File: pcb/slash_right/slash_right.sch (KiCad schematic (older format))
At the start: 6 parts

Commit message: pcb: slash_right: General electronics
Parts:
- added C? (x5): 100n, symbol Device:C
- added C? (x2): 22p, symbol Device:C_Small
- added C?: 1u, symbol Device:C
- added C?: CP, symbol Device:CP
- added D?: D_Small, symbol Device:D_Small
- added D?: LED, symbol Device:LED
- added R? (x2): 10K, symbol Device:R_Small
- added R? (x2): 22, symbol Device:R_Small
- added R?: 470, symbol Device:R_Small
- added R? (x2): 4.7K, symbol Device:R_Small
- added SW?: SW_Push, symbol Switch:SW_Push
- added U?: ATmega32U4-AU, Package_QFP:TQFP-44_10x10mm_P0.8mm, symbol MCU_Microchip_ATmega:ATmega32U4-AU
- added Y?: 16MHz, symbol Device:Crystal
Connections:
- net +5V: now also J?.3, C?.1, C?.1, C?.1, C?.1, C?.1, C?.1, D?.1 (K), R?.1, R?.1, R?.1, U?.14 (VCC), U?.2 (UVCC), U?.24 (AVCC), U?.34 (VCC), U?.44 (AVCC), U?.7 (VBUS)
- net D+: now also R?.2
- net D-: now also R?.2
- net GND: now also J?.5, C?.1, C?.2, C?.2, C?.2, C?.2, C?.2, C?.2, C?.2, C?.2, D?.1 (K), R?.1, SW?.1, U?.15 (GND), U?.23 (GND), U?.35 (GND), U?.43 (GND), U?.5 (UGND)
- net SCL: now also J?.4, R?.2, U?.18 (PD0)
- net SDA: now also J?.2, R?.2, U?.19 (PD1)
- net MISO: now reaches J?.1 (MISO)
- net MISO: now also U?.11 (PB3)
- net SCK: now reaches J?.3 (SCK)
- net SCK: now also U?.9 (PB1)
- net MOSI: now reaches J?.4 (MOSI)
- net MOSI: now also U?.10 (PB2)
- net ~RST: now reaches J?.5 (~RST)
- net ~RST: now also D?.2 (A), R?.2, SW?.2, U?.13 (~RESET)
- new net: R?.1, U?.1 (PE6)
- new net: C?.2, U?.16 (XTAL2), Y?.2
- new net: C?.1, U?.17 (XTAL1), Y?.1
- new net: R?.2, U?.33 (~HWB~/PE2)
- new net: C?.1, U?.6 (UCAP)
- new net: D?.2 (A), R?.2
- new net D1+: R?.1, U?.4 (D+)
- new net D1-: R?.1, U?.3 (D-)
- no-connect marks 3 -> 4

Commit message: pcb: slash: Matrix schematic
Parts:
- added D? (x55): D_Small, symbol Device:D_Small
- added SW? (x55): SW_Push_45deg, symbol Switch:SW_Push_45deg
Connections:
- net COL7: now reaches U?.12 (PB7)
- net COL7: now also SW?.2, SW?.2, SW?.2
- net COL10: now reaches U?.20 (PD2)
- net COL10: now also SW?.2, SW?.2, SW?.2
- net COL11: now reaches U?.21 (PD3)
- net COL11: now also SW?.2, SW?.2, SW?.2
- net COL13: now reaches U?.22 (PD5)
- net COL13: now also SW?.2, SW?.2, SW?.2
- net COL12: now reaches U?.25 (PD4)
- net COL12: now also SW?.2, SW?.2, SW?.2
- net COL14: now reaches U?.26 (PD6)
- net COL14: now also SW?.2, SW?.2, SW?.2
- net COL15: now reaches U?.27 (PD7)
- net COL15: now also SW?.2, SW?.2, SW?.2
- net COL4: now reaches U?.28 (PB4)
- net COL4: now also SW?.2, SW?.2, SW?.2
- net COL5: now reaches U?.29 (PB5)
- net COL5: now also SW?.2, SW?.2, SW?.2
- net COL6: now reaches U?.30 (PB6)
- net COL6: now also SW?.2, SW?.2, SW?.2
- net COL8: now reaches U?.31 (PC6)
- net COL8: now also SW?.2, SW?.2, SW?.2
- net COL9: now reaches U?.32 (PC7)
- net COL9: now also SW?.2, SW?.2, SW?.2
- net ROW2: now reaches U?.36 (PF7)
- net ROW2: now also D?.1 (K), D?.1 (K), D?.1 (K), D?.1 (K), D?.1 (K), D?.1 (K), D?.1 (K), D?.1 (K), D?.1 (K), D?.1 (K), D?.1 (K), D?.1 (K), D?.1 (K), D?.1 (K), D?.1 (K), D?.1 (K), D?.1 (K), D?.1 (K), D?.1 (K)
- net ROW1: now reaches U?.37 (PF6)
- net ROW1: now also D?.1 (K), D?.1 (K), D?.1 (K), D?.1 (K), D?.1 (K), D?.1 (K), D?.1 (K), D?.1 (K), D?.1 (K), D?.1 (K), D?.1 (K), D?.1 (K), D?.1 (K), D?.1 (K), D?.1 (K), D?.1 (K), D?.1 (K)
- net ROW0: now reaches U?.38 (PF5)
- net ROW0: now also D?.1 (K), D?.1 (K), D?.1 (K), D?.1 (K), D?.1 (K), D?.1 (K), D?.1 (K), D?.1 (K), D?.1 (K), D?.1 (K), D?.1 (K), D?.1 (K), D?.1 (K), D?.1 (K), D?.1 (K), D?.1 (K), D?.1 (K), D?.1 (K), D?.1 (K)
- net COL18: now reaches U?.39 (PF4)
- net COL18: now also SW?.2, SW?.2
- net COL17: now reaches U?.40 (PF1)
- net COL17: now also SW?.2, SW?.2, SW?.2
- net COL16: now reaches U?.41 (PF0)
- net COL16: now also SW?.2, SW?.2
- net COL0: now reaches U?.8 (PB0)
- net COL0: now also SW?.2, SW?.2, SW?.2
- net MISO renamed COL3
- net COL3: now also SW?.2, SW?.2, SW?.2
- net MOSI renamed COL2
- net COL2: now also SW?.2, SW?.2, SW?.2
- net SCK renamed COL1
- net COL1: now also SW?.2, SW?.2, SW?.2
- new net: D?.2 (A), SW?.1 (x55)

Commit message: pcb: slash_righ: Fill missing values
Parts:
- C?: value CP -> 10uF
- F?: value Polyfuse -> 500mA
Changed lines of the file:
@@
 P 1450 950
 F 0 "F?" V 1225 950 50  0000 C CNN
-F 1 "Polyfuse" V 1316 950 50  0000 C CNN
+F 1 "500mA" V 1316 950 50  0000 C CNN
 F 2 "" H 1500 750 50  0001 L CNN
 F 3 "~" H 1450 950 50  0001 C CNN
@@
 P 1900 4650
 F 0 "C?" H 2018 4696 50  0000 L CNN
-F 1 "CP" H 2018 4605 50  0000 L CNN
+F 1 "10uF" H 2018 4605 50  0000 L CNN
 F 2 "" H 1938 4500 50  0001 C CNN
 F 3 "~" H 1900 4650 50  0001 C CNN

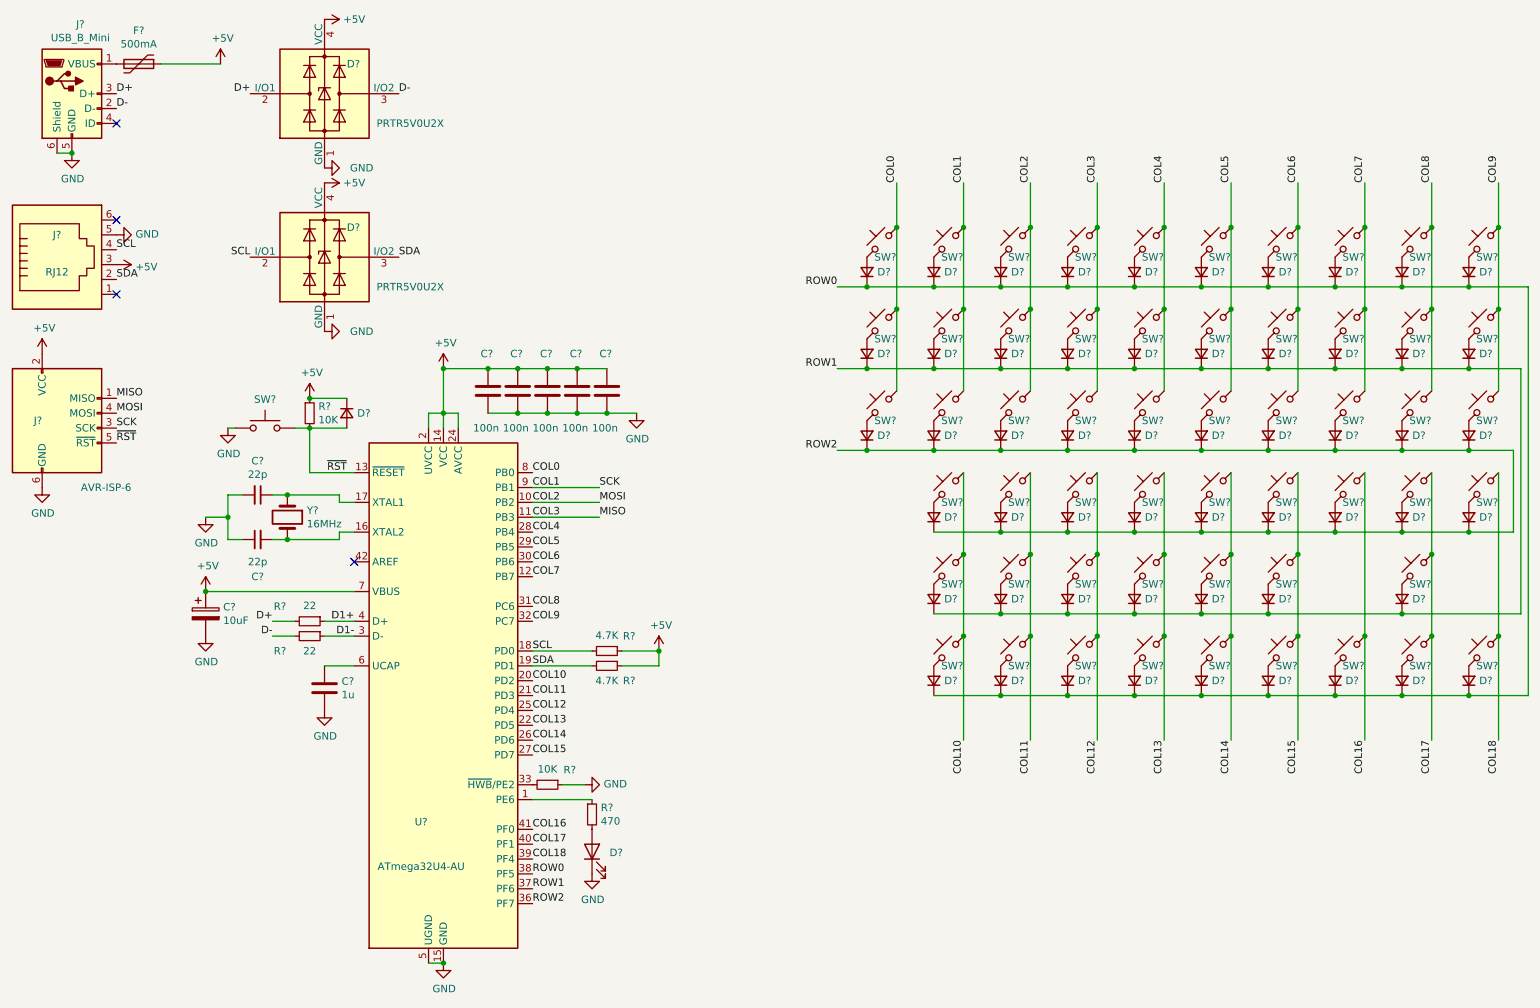
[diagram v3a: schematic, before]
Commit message: pcb: slash_right: Annotate
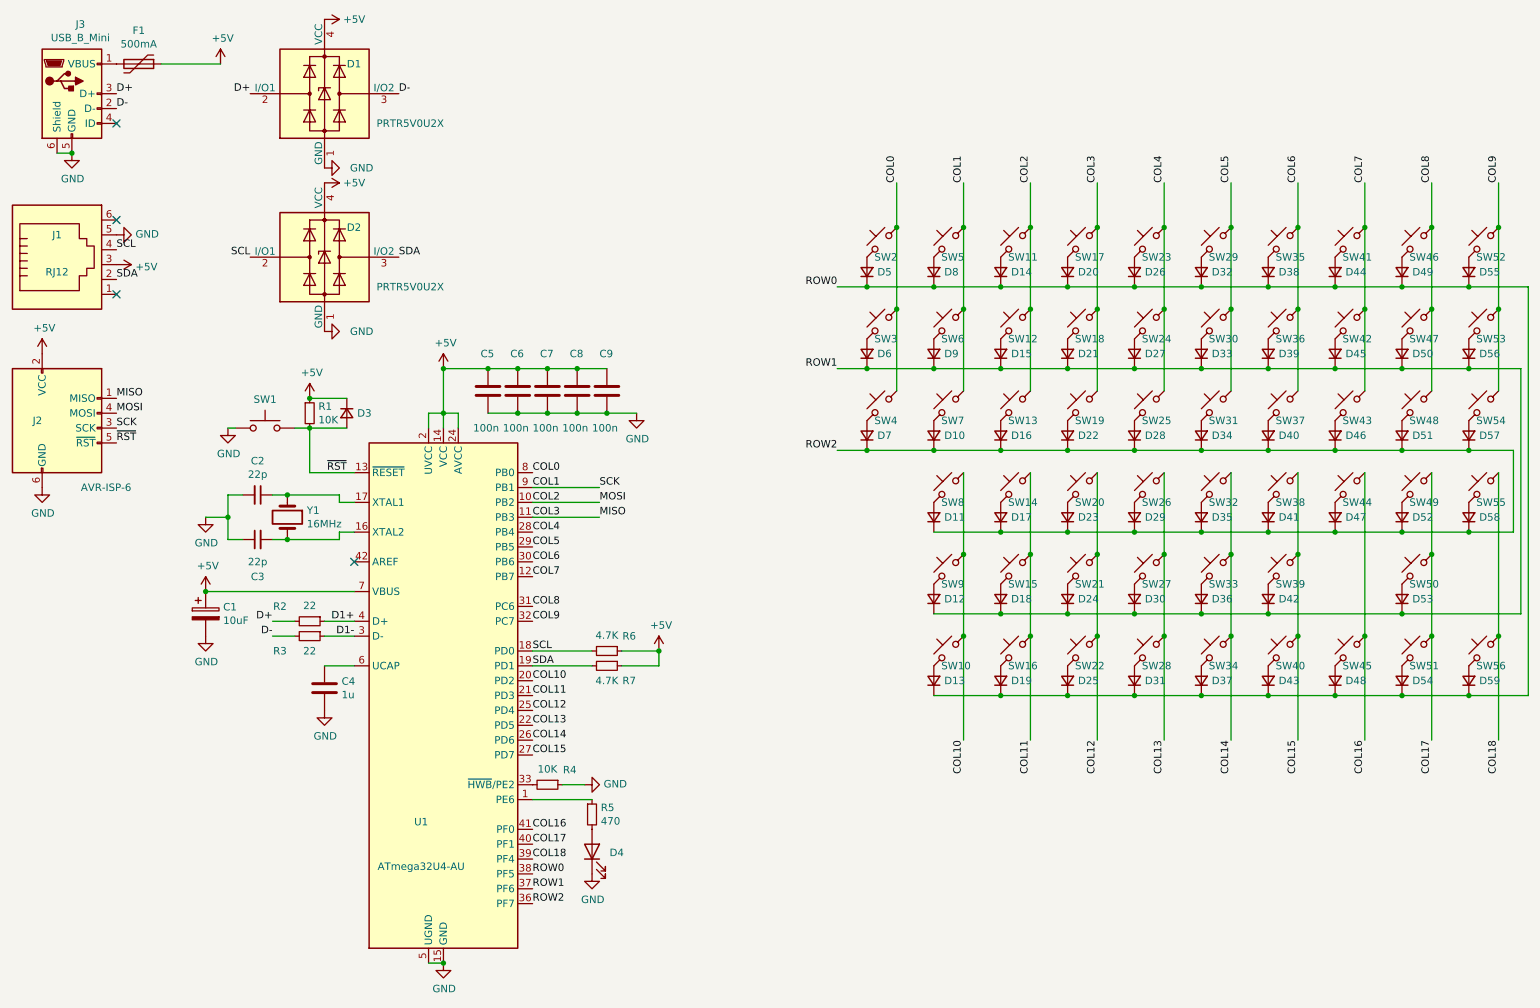
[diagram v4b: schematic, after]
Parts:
- gave numbers to parts that had none: 137

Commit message: pcb: slash_right: Assign footprints
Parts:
- C1: footprint (none) -> Capacitor_Tantalum_SMD:CP_EIA-3216-18_Kemet-A_Pad1.58x1.35mm_HandSolder
- C2, C3, C4, C5, C6, C7, C8, C9: footprint (none) -> Capacitor_SMD:C_0805_2012Metric_Pad1.18x1.45mm_HandSolder
- D10, D11, D12, D13, D14, D15, D16, D17, D18, D19, D20, D21, D22, D23, D24, D25, D26, D27, D28, D29, D3, D30, D31, D32, D33, D34, D35, D36, D37, D38, D39, D40, D41, D42, D43, D44, D45, D46, D47, D48, D49, D5, D50, D51, D52, D53, D54, D55, D56, D57, D58, D59, D6, D7, D8, D9: footprint (none) -> Diode_SMD:D_SOD-123
- D4: footprint (none) -> LED_SMD:LED_0805_2012Metric_Pad1.15x1.40mm_HandSolder
- F1: footprint (none) -> Fuse:Fuse_0805_2012Metric_Pad1.15x1.40mm_HandSolder
- J1: footprint (none) -> local_footprint:RJ12_Custom1
- J2: footprint (none) -> Connector_PinHeader_2.54mm:PinHeader_2x03_P2.54mm_Vertical
- J3: footprint (none) -> local_footprint:USB_Mini-B_Custom1_Horizontal
- R1, R2, R3, R4, R5, R6, R7: footprint (none) -> Resistor_SMD:R_0805_2012Metric_Pad1.20x1.40mm_HandSolder
- SW1: footprint (none) -> Button_Switch_THT:SW_PUSH_6mm_H4.3mm
- SW10, SW11, SW12, SW13, SW14, SW15, SW16, SW17, SW18, SW19, SW2, SW20, SW21, SW22, SW23, SW24, SW25, SW26, SW27, SW28, SW29, SW3, SW30, SW31, SW32, SW33, SW34, SW35, SW36, SW37, SW38, SW39, SW4, SW40, SW41, SW42, SW43, SW44, SW45, SW46, SW47, SW48, SW49, SW5, SW50, SW51, SW52, SW53, SW54, SW55, SW56, SW6, SW7, SW8, SW9: footprint (none) -> keyswitches:Kailh_socket_MX
- Y1: footprint (none) -> Crystal:Crystal_HC49-U_Vertical

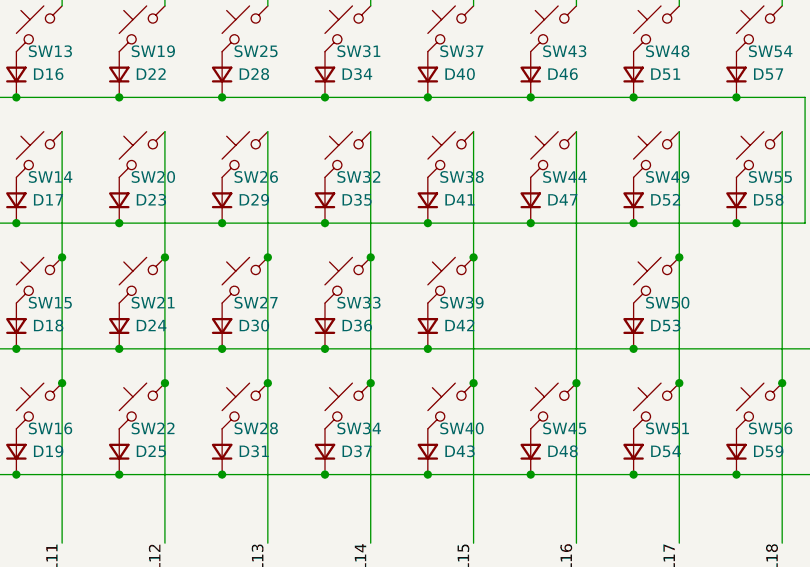
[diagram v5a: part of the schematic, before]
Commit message: pcb: slash_righ: Place switches
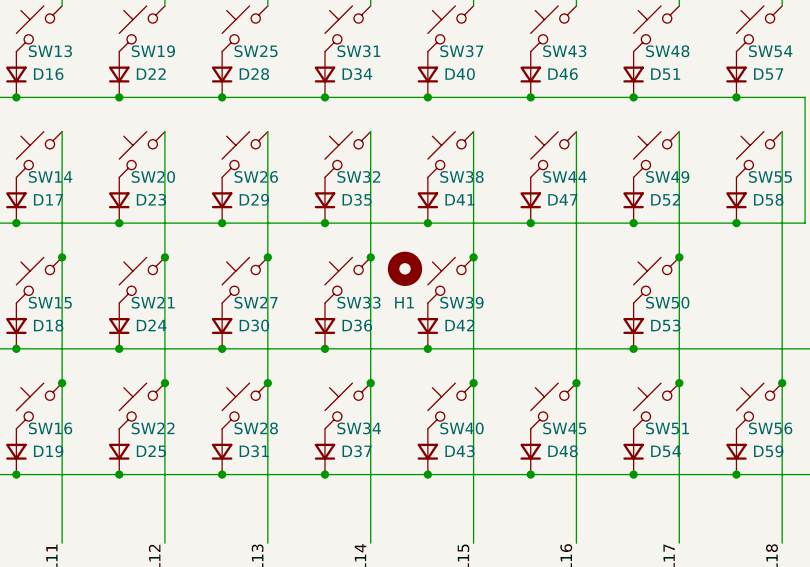
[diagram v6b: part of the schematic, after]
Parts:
- added H1: MountingHole, keyswitches:Stabilizer_MX_2u, symbol Mechanical:MountingHole
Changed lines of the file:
@@
 Text Label 4100 6600 0    50   ~ 0
 ROW2
+$Comp
+L Mechanical:MountingHole H1
+U 1 1 61859E36
+P 8950 4300
+F 0 "H1" H 8900 4150 50  0000 L CNN
+F 1 "MountingHole" H 9050 4255 50  0001 L CNN
+F 2 "keyswitches:Stabilizer_MX_2u" H 8950 4300 50  0001 C CNN
+F 3 "~" H 8950 4300 50  0001 C CNN
+	1    8950 4300
+	1    0    0    -1
+$EndComp
 $EndSCHEMATC

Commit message: pcb: slash_right: Add PWR symbol
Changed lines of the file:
@@
 $EndComp
 Wire Wire Line
-	2000 950  1600 950
+	2000 950  1750 950
 Text Label 1300 1150 0    50   ~ 0
 D+
@@
 	1    0    0    -1
 $EndComp
+$Comp
+L power:PWR_FLAG #FLG0101
+U 1 1 6193F379
+P 1750 950
+F 0 "#FLG0101" H 1750 1025 50  0001 C CNN
+F 1 "PWR_FLAG" H 1750 1123 50  0000 C CNN
+F 2 "" H 1750 950 50  0001 C CNN
+F 3 "~" H 1750 950 50  0001 C CNN
+	1    1750 950
+	1    0    0    -1
+$EndComp
+Connection ~ 1750 950
+Wire Wire Line
+	1750 950  1600 950
 $EndSCHEMATC

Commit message: pcb: slash: Progress
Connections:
- net COL1: now also U1.41 (PF0); no longer J2.3 (SCK), U1.9 (PB1)
- net COL16: now also J2.3 (SCK), U1.9 (PB1); no longer U1.41 (PF0)
- net COL17: now also J2.4 (MOSI), U1.10 (PB2); no longer U1.40 (PF1)
- net COL18: now also J2.1 (MISO), U1.11 (PB3); no longer U1.39 (PF4)
- net COL2: now also U1.40 (PF1); no longer J2.4 (MOSI), U1.10 (PB2)
- net COL3: now also U1.39 (PF4); no longer J2.1 (MISO), U1.11 (PB3)
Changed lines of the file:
@@
 Text Label 4100 3700 0    50   ~ 0
 COL0
-Text Label 4100 3800 0    50   ~ 0
+Text Label 4100 6100 0    50   ~ 0
 COL1
-Text Label 4100 3900 0    50   ~ 0
+Text Label 4100 6200 0    50   ~ 0
 COL2
-Text Label 4100 4000 0    50   ~ 0
+Text Label 4100 6300 0    50   ~ 0
 COL3
 Text Label 4100 4100 0    50   ~ 0
@@
 Text Label 4100 5600 0    50   ~ 0
 COL15
-Text Label 4100 6100 0    50   ~ 0
-COL16
-Text Label 4100 6200 0    50   ~ 0
-COL17
-Text Label 4100 6300 0    50   ~ 0
-COL18
 Connection ~ 10150 4250
 Wire Wire Line
@@
 Wire Wire Line
 	1750 950  1600 950
+Text Label 4100 3800 0    50   ~ 0
+COL16
+Text Label 4100 3900 0    50   ~ 0
+COL17
+Text Label 4100 4000 0    50   ~ 0
+COL18
 $EndSCHEMATC
